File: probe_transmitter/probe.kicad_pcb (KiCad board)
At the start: 2 copper layers, 28 x 28 mm, 36 parts, among them Q1 PMST2222, U1 ATtiny85-20M

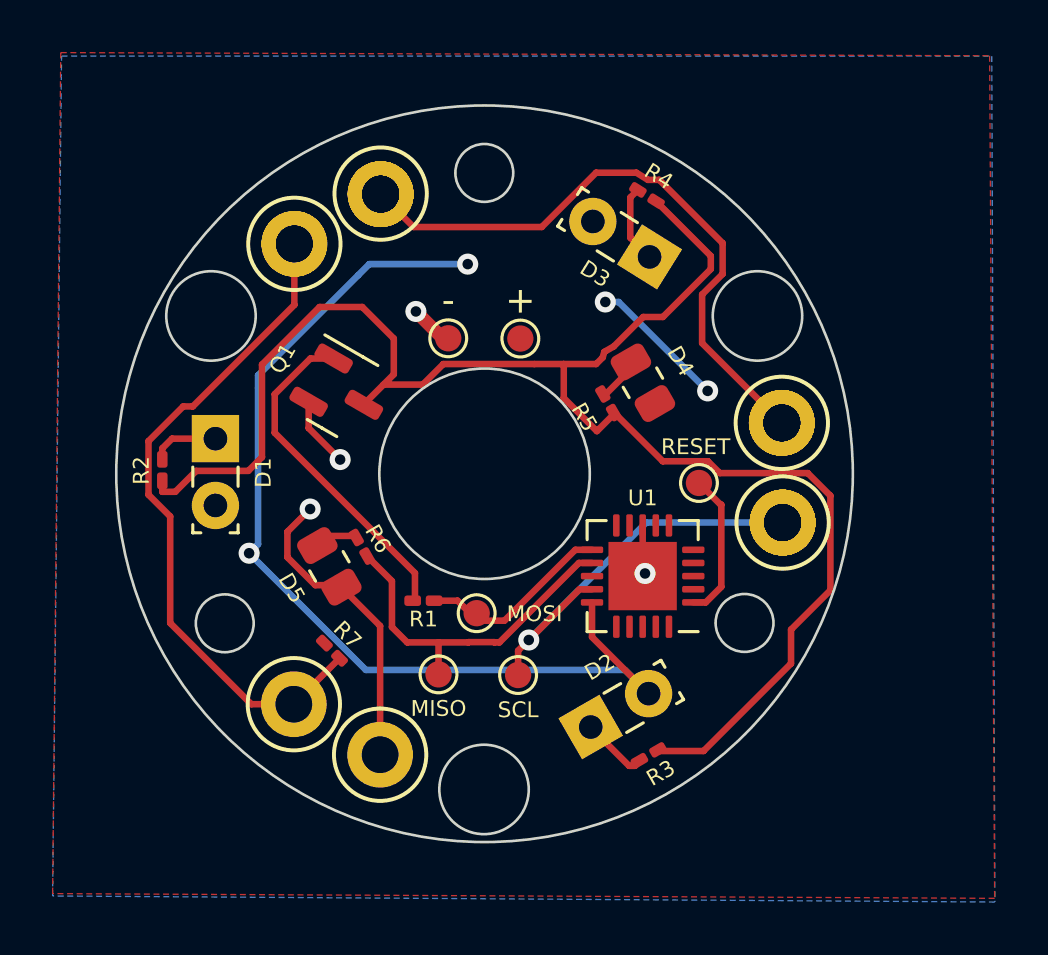
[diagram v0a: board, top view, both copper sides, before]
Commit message: - add fix for PCB v1.1 (fix resistor place 1608)
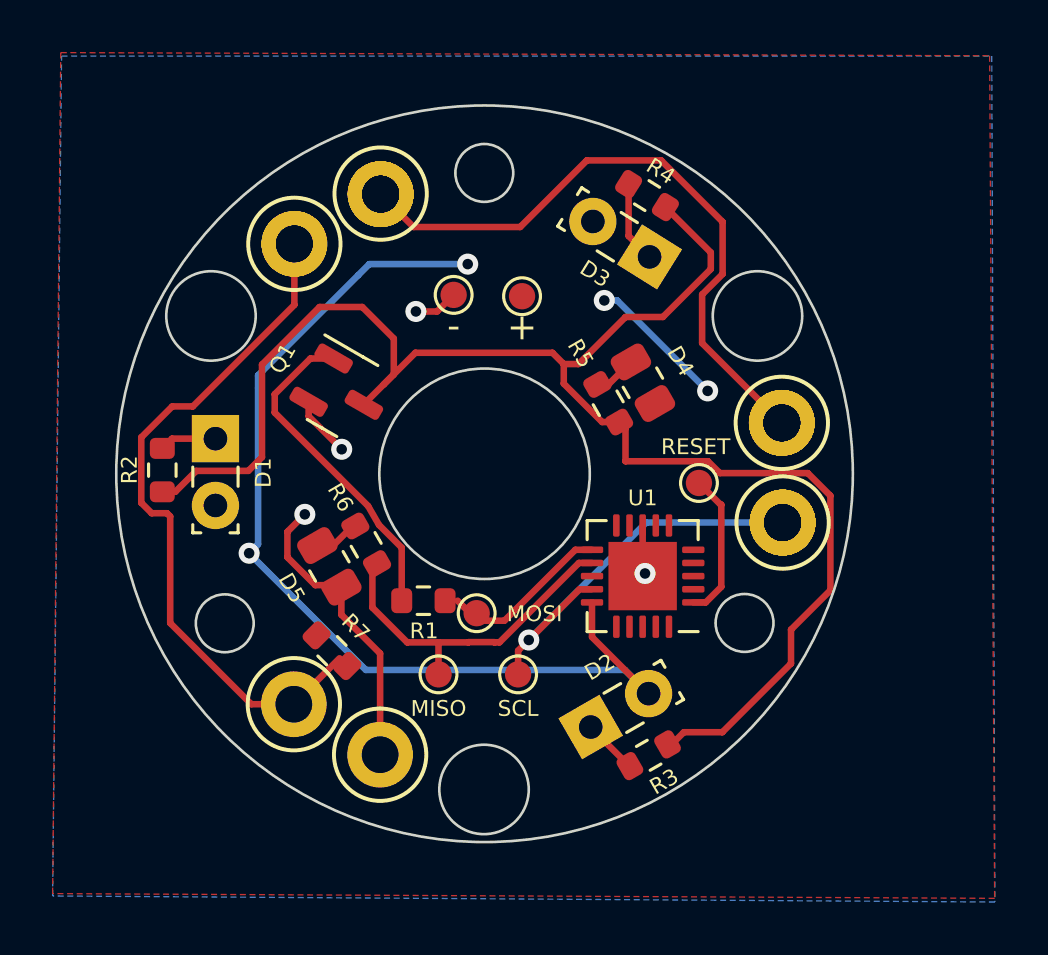
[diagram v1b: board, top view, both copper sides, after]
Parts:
- added  : Touch Probe v1.1, LOGO, B.Cu at (99.4, 92.8)
- R1, R2, R3, R4, R5, R6, R7: footprint Resistor_SMD:R_0201_0603Metric_Pad0.64x0.40mm_HandSolder -> Resistor_SMD:R_0603_1608Metric
- moved - 1.66 mm to (98.8, 93.2)
- moved + 1.61 mm to (101.4, 93.2)
- moved R6 0.19 mm to (95.5, 102.7)
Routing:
- net /PAD1: track 67.5 -> 69.3 mm
- net Net-(Q1-Pad3): track 62.8 -> 61.3 mm
- net Net-(MOSI-Pad1): track 7.52 -> 6.54 mm
- net GND: track 17.9 -> 17.3 mm
- net Net-(D5-Pad2): track 1.52 -> 2.06 mm
- net Net-(D1-Pad1): track 2.68 -> 2.17 mm

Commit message: - update probe transmitter
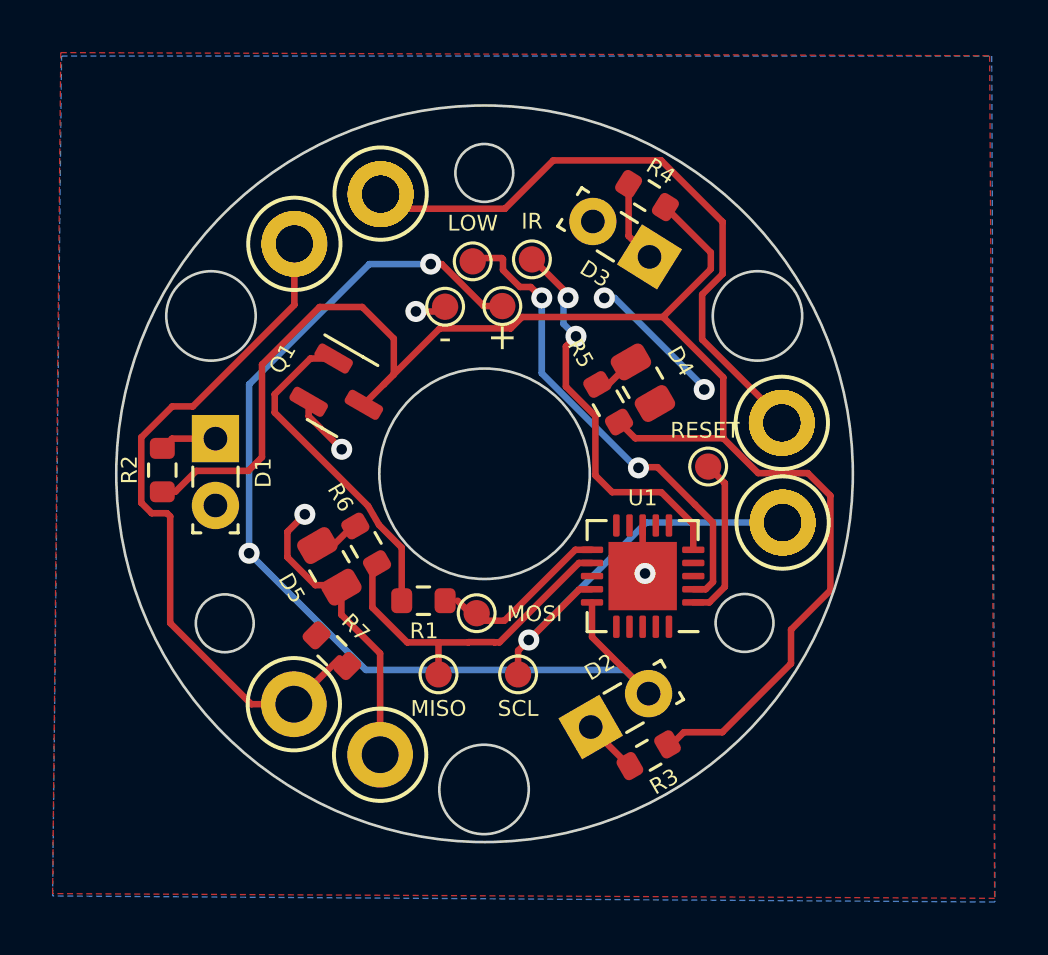
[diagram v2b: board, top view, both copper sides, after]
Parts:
- added IR: PB4, TestPoint:TestPoint_Pad_D1.0mm, F.Cu at (101.8, 91.8)
- added LOW: PB3, TestPoint:TestPoint_Pad_D1.0mm, F.Cu at (99.5, 91.9)
- moved + 0.84 mm to (100.7, 93.6)
- moved RESET 0.72 mm to (108.5, 99.7)
- moved - 0.56 mm to (98.5, 93.7)
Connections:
- U1 pad 2: unconnected-(U1-Pad2) -> Net-(U1-Pad2)
- U1 pad 5: unconnected-(U1-Pad5) -> Net-(U1-Pad5)
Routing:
- net Net-(U1-Pad2): track 0.00 -> 18.3 mm, vias 0 -> 2
- net Net-(U1-Pad5): track 0.00 -> 15.2 mm, vias 0 -> 2
- net +3.3V: track 43.7 -> 45.6 mm
- net Net-(Q1-Pad3): track 61.3 -> 62.3 mm
- net Net-(U1-Pad1): track 5.62 -> 6.28 mm
- net /PAD1: track 69.3 -> 68.7 mm
- net GND: track 17.3 -> 16.8 mm

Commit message: - v .1.1 in prode
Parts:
- removed the ? at (111.3, 101.9) (x3)
- removed the ? at (96.0, 110.7)
- removed the ? at (96.0, 89.4) (x4)
- removed the ? at (92.8, 91.3) (x2)
- removed the ? at (111.3, 98.1) (x3)
- removed the ? at (92.8, 108.8)
- added 1: , , F.Cu at (92.7, 91.2)
- added 2: , , F.Cu at (96.0, 89.3)
- added 3: , , F.Cu at (96.0, 110.8)
- added 4: , , F.Cu at (92.7, 108.9)
- moved U1 0.29 mm to (105.7, 103.9)
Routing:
- net /PAD1: track 68.7 -> 67.9 mm
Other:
- outline, holes or cut-outs redrawn

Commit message: - add new power version
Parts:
- removed D1, D2, D3: IRL81A, LED_THT:LED_SideEmitter_Rectangular_W4.5mm_H1.6mm
- removed R3, R4: R39, Resistor_SMD:R_0603_1608Metric
- added IR_LED1: PB4, TestPoint:TestPoint_Pad_D1.0mm, F.Cu at (103.6, 87.5)
- added Q2: PMST2222, Package_TO_SOT_SMD:SOT-23, F.Cu at (88.7, 100.9)
-  : value Touch Probe v1.1 -> Touch Probe v1.2
- moved D5 14.3 mm to (105.1, 94.4), turned to 0 degrees
- moved R5 11.8 mm to (92.9, 97.5), turned to -90 degrees
- moved R6 11.6 mm to (101.7, 93.0), turned to 0 degrees
- moved - 11.4 mm to (109.6, 91.3)
- moved R1 9.68 mm to (91.4, 97.5), turned to 90 degrees
- moved + 8.44 mm to (108.3, 90.1)
- moved LOW1 6.89 mm to (105.3, 88.2)
- moved   6.30 mm to (105.6, 91.7)
- moved Q1 5.95 mm to (88.7, 97.5), turned to 0 degrees
- moved IR1 5.82 mm to (106.9, 89.0)
- moved U1 5.38 mm to (104.6, 109.2), turned to 45 degrees
- moved RES 4.48 mm to (105.3, 102.9)
- moved D4 4.35 mm to (105.1, 92.3), turned to 0 degrees
- moved SCL 4.22 mm to (104.1, 104.5)
- moved R2 3.80 mm to (91.4, 100.9), turned to -90 degrees
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- renumbered IR to IR1, LOW to LOW1, RESET to RES
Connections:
- IR1 pad 1: Net-(U1-Pad5) -> Net-(IR1-Pad1)
- Q1 pad 3: Net-(Q1-Pad3) -> Net-(IR_LED1-Pad1)
- R2 pad 1: Net-(Q1-Pad3) -> Net-(R2-Pad1)
- R5 pad 1: Net-(Q1-Pad3) -> Net-(IR_LED1-Pad1)
- U1 pad 5: Net-(U1-Pad5) -> Net-(R2-Pad1)
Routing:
- net Net-(Q1-Pad3): track 62.3 -> 0.00 mm
- net Net-(IR1-Pad1): track 0.00 -> 28.5 mm, vias 0 -> 2
- net Net-(IR_LED1-Pad1): track 0.00 -> 26.0 mm
- net GND: track 16.8 -> 40.9 mm, vias 4 -> 3
- net Net-(MISO1-Pad1): track 13.0 -> 33.6 mm, vias 0 -> 3
- net Net-(R2-Pad1): track 0.00 -> 18.8 mm
- net Net-(MOSI1-Pad1): track 6.54 -> 24.4 mm, vias 0 -> 2
- net Net-(U1-Pad5): track 15.2 -> 0.00 mm, vias 2 -> 0
- net Net-(D4-Pad1): track 1.90 -> 14.0 mm
- net Net-(Q1-Pad1): track 12.6 -> 3.70 mm
- net Net-(LOW1-Pad1): track 17.9 -> 26.0 mm
- net Net-(RESET1-Pad1): track 6.24 -> 11.6 mm, vias 0 -> 2
- net /PAD1: track 67.9 -> 63.4 mm, vias 1 -> 0
- net Net-(D3-Pad1): track 3.18 -> 0.00 mm
- net Net-(Q2-Pad1): track 2.17 -> 4.65 mm
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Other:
- board size 28 x 28 mm -> 28.4 x 28.4 mm

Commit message: -add new version for transmitter
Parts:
- removed +, -: , TestPoint:TestPoint_Pad_D1.0mm
- removed IR1, IR_LED1: PB4, TestPoint:TestPoint_Pad_D1.0mm
- removed LOW1: PB3, TestPoint:TestPoint_Pad_D1.0mm
- removed U1: ATtiny85-20M, Package_DFN_QFN:QFN-20-1EP_4x4mm_P0.5mm_EP2.6x2.6mm
- added J2: Conn_01x06, Connector_FFC-FPC:TE_0-1734839-6_1x06-1MP_P0.5mm_Horizontal, B.Cu at (103.8, 93.6)
- added U2: ATtiny84-20M, Package_DFN_QFN:QFN-20-1EP_4x4mm_P0.5mm_EP2.6x2.6mm, F.Cu at (104.8, 106.7)
-  : value Touch Probe v1.2 -> Touch Probe v1.4
- moved   16.7 mm to (91.0, 99.8)
- moved D5 13.5 mm to (99.9, 106.9), turned to -90 degrees
- moved R6 12.4 mm to (92.7, 101.5), turned to 90 degrees
- moved RES1 9.89 mm to (103.8, 112.7), turned to 180 degrees
- moved MISO1 8.75 mm to (107.9, 110.6), turned to 180 degrees
- moved MOSI1 7.15 mm to (106.0, 111.8), turned to 180 degrees
- moved SCL1 7.13 mm to (109.6, 109.0), turned to 180 degrees
- moved D4 5.09 mm to (100.0, 93.2), turned to 90 degrees
- moved R7 1.59 mm to (93.3, 104.8), turned to 0 degrees
- moved Q1 0.65 mm to (88.4, 98.0)
- moved Q2 0.65 mm to (88.4, 101.5)
- moved R1 0.65 mm to (91.1, 98.0)
- moved R2 0.65 mm to (91.1, 101.5), turned to 90 degrees
- moved R5 0.60 mm to (92.7, 98.0)
- renumbered MISO to MISO1, MOSI to MOSI1, RES to RES1, SCL to SCL1
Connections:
- MISO1 pad 1: Net-(MISO1-Pad1) -> Net-(U2-PA5)
- MOSI1 pad 1: Net-(MOSI1-Pad1) -> Net-(U2-PA6)
- R1 pad 1: Net-(MOSI1-Pad1) -> Net-(U2-XTAL1/PB0)
- R6 pad 1: Net-(MISO1-Pad1) -> Net-(U2-XTAL2/PB1)
- SCL1 pad 1: /PAD1 -> Net-(U2-PA4)
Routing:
- net Net-(MISO1-Pad1): track 33.6 -> 0.00 mm, vias 3 -> 0
- net Net-(U2-PA3): track 18.8 -> 45.1 mm, vias 0 -> 2
- net Net-(LOW1-Pad1): track 26.0 -> 0.00 mm, vias 2 -> 0
- net Net-(J2-Pin_5): track 0.00 -> 24.5 mm, vias 0 -> 1
- net Net-(MOSI1-Pad1): track 24.4 -> 0.00 mm, vias 2 -> 0
- net Net-(U2-XTAL1/PB0): track 0.00 -> 20.3 mm
- net Net-(J2-Pin_4): track 0.00 -> 19.5 mm, vias 0 -> 1
- net Net-(U2-XTAL2/PB1): track 0.00 -> 16.1 mm
- net +3.3V: track 43.6 -> 31.4 mm
- net GND: track 40.9 -> 28.8 mm, vias 3 -> 2
- net Net-(D5-A): track 4.05 -> 12.1 mm, vias 0 -> 2
- net Net-(J2-Pin_2): track 26.0 -> 19.4 mm, vias 0 -> 1
- net /PAD1: track 63.4 -> 69.8 mm, vias 0 -> 1
- net Net-(U2-~{RESET}/PB3): track 11.6 -> 5.77 mm, vias 2 -> 0
- net Net-(D4-K): track 14.0 -> 9.33 mm
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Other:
- board size 28.4 x 28.4 mm -> 28.5 x 28.5 mm
